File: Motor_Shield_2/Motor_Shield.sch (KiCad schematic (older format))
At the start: 49 parts, among them J1 Conn_01x08_Female, J10 Conn_01x02_Male, J11 Conn_01x02_Male, J12 Conn_01x02_Male, J13 Conn_01x02_Male, J14 Conn_01x02_Male, J15 Conn_01x02_Male, J16 Conn_01x02_Male, J17 Conn_01x02_Male, J18 Conn_01x02_Male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

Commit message: Überarbeiten das Pin Header schlecht plaziert waren
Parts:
- removed D4, D5, D6, D7: LED, Diode_SMD:D_1206_3216Metric, symbol Device:LED
- removed R22, R23, R24, R25: 2.2k, Resistor_SMD:R_1206_3216Metric_Pad1.42x1.75mm_HandSolder, symbol Device:R
- added J23: Conn_01x04_Female, Connector_PinHeader_2.54mm:PinHeader_1x04_P2.54mm_Vertical, symbol Connector:Conn_01x04_Female
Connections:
- net at J6.3 (Pin_3), U1.17 (OUT1B), U1.18 (OUT1B): now also J23.3 (Pin_3)
- net at J6.5 (Pin_5), U1.2 (OUT1A), U1.3 (OUT1A): now also J23.1 (Pin_1)
- net at J6.4 (Pin_4), U1.20 (OUT2B), U1.21 (OUT2B): now also J23.4 (Pin_4)
- net at J6.6 (Pin_6), U1.35 (OUT2A), U1.36 (OUT2A): now also J23.2 (Pin_2)
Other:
- note added: "Debug_PL Anschluss"
- note added: "J7\n\nJ12\n\nJ17\n\nJ20"
- note added: "J8\n\nJ13\n\nJ18\n\nJ21"
- note added: "J9\n\nJ14\n\nJ19\n\nJ22\n"
- note removed: "R1\n\nR4\n\nR7\n\nR10"
- note removed: "R2\n\nR5\n\nR8\n\nR11"
- note removed: "R3\n\nR6\n\nR9\n\nR12"
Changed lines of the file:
@@
 EESchema Schematic File Version 4
+LIBS:Motor_Shield-cache
 EELAYER 30 0
 EELAYER END
@@
 	6800 3850 6600 3850
 Wire Wire Line
-	6600 4050 6800 4050
-Wire Wire Line
-	6800 4050 6800 4150
-Wire Wire Line
-	6800 4150 6600 4150
-Wire Wire Line
-	6800 3000 6850 3000
-Wire Wire Line
 	8050 3000 8050 2700
 Wire Wire Line
@@
 Connection ~ 6800 3000
 Wire Wire Line
-	6800 3200 7200 3200
-Wire Wire Line
-	8150 3200 8150 2800
+	8150 3200 8150 3100
 Connection ~ 6800 3200
 Wire Wire Line
-	6800 3750 7550 3750
-Wire Wire Line
-	7900 3750 7900 2500
+	7900 3750 7900 3250
 Wire Wire Line
 	7900 2500 8150 2500
 Connection ~ 6800 3750
 Wire Wire Line
-	8000 4050 8000 2600
-Wire Wire Line
 	8000 2600 8150 2600
-Wire Wire Line
-	6800 4050 7900 4050
-Connection ~ 6800 4050
-$Comp
-L Device:LED D4
-U 1 1 5E5AB89E
-P 6850 4450
-F 0 "D4" V 6889 4333 50  0000 R CNN
-F 1 "LED" V 6798 4333 50  0000 R CNN
-F 2 "Diode_SMD:D_1206_3216Metric" H 6850 4450 50  0001 C CNN
-F 3 "~" H 6850 4450 50  0001 C CNN
-	1    6850 4450
-	0    -1   -1   0
-$EndComp
-$Comp
-L Device:R R22
-U 1 1 5E5AD872
-P 6850 4850
-F 0 "R22" V 6643 4850 50  0000 C CNN
-F 1 "2.2k" V 6734 4850 50  0000 C CNN
-F 2 "Resistor_SMD:R_1206_3216Metric_Pad1.42x1.75mm_HandSolder" V 6780 4850 50  0001 C CNN
-F 3 "~" H 6850 4850 50  0001 C CNN
-	1    6850 4850
-	-1   0    0    1
-$EndComp
-$Comp
-L power:GND #PWR019
-U 1 1 5E5AF353
-P 6850 5100
-F 0 "#PWR019" H 6850 4850 50  0001 C CNN
-F 1 "GND" H 6855 4927 50  0000 C CNN
-F 2 "" H 6850 5100 50  0001 C CNN
-F 3 "" H 6850 5100 50  0001 C CNN
-	1    6850 5100
-	1    0    0    -1
-$EndComp
-Wire Wire Line
-	6850 5100 6850 5000
-Wire Wire Line
-	6850 4700 6850 4600
-$Comp
-L Device:LED D5
-U 1 1 5E5B4D77
-P 7200 4450
-F 0 "D5" V 7239 4333 50  0000 R CNN
-F 1 "LED" V 7148 4333 50  0000 R CNN
-F 2 "Diode_SMD:D_1206_3216Metric" H 7200 4450 50  0001 C CNN
-F 3 "~" H 7200 4450 50  0001 C CNN
-	1    7200 4450
-	0    -1   -1   0
-$EndComp
-$Comp
-L Device:R R23
-U 1 1 5E5B4D7D
-P 7200 4850
-F 0 "R23" V 6993 4850 50  0000 C CNN
-F 1 "2.2k" V 7084 4850 50  0000 C CNN
-F 2 "Resistor_SMD:R_1206_3216Metric_Pad1.42x1.75mm_HandSolder" V 7130 4850 50  0001 C CNN
-F 3 "~" H 7200 4850 50  0001 C CNN
-	1    7200 4850
-	-1   0    0    1
-$EndComp
-$Comp
-L power:GND #PWR021
-U 1 1 5E5B4D83
-P 7200 5100
-F 0 "#PWR021" H 7200 4850 50  0001 C CNN
-F 1 "GND" H 7205 4927 50  0000 C CNN
-F 2 "" H 7200 5100 50  0001 C CNN
-F 3 "" H 7200 5100 50  0001 C CNN
-	1    7200 5100
-	1    0    0    -1
-$EndComp
-Wire Wire Line
-	7200 5100 7200 5000
-Wire Wire Line
-	7200 4700 7200 4600
-$Comp
-L Device:LED D6
-U 1 1 5E5B6E4B
-P 7550 4450
-F 0 "D6" V 7589 4333 50  0000 R CNN
-F 1 "LED" V 7498 4333 50  0000 R CNN
-F 2 "Diode_SMD:D_1206_3216Metric" H 7550 4450 50  0001 C CNN
-F 3 "~" H 7550 4450 50  0001 C CNN
-	1    7550 4450
-	0    -1   -1   0
-$EndComp
-$Comp
-L Device:R R24
-U 1 1 5E5B6E51
-P 7550 4850
-F 0 "R24" V 7343 4850 50  0000 C CNN
-F 1 "2.2k" V 7434 4850 50  0000 C CNN
-F 2 "Resistor_SMD:R_1206_3216Metric_Pad1.42x1.75mm_HandSolder" V 7480 4850 50  0001 C CNN
-F 3 "~" H 7550 4850 50  0001 C CNN
-	1    7550 4850
-	-1   0    0    1
-$EndComp
-$Comp
-L power:GND #PWR023
-U 1 1 5E5B6E57
-P 7550 5100
-F 0 "#PWR023" H 7550 4850 50  0001 C CNN
-F 1 "GND" H 7555 4927 50  0000 C CNN
-F 2 "" H 7550 5100 50  0001 C CNN
-F 3 "" H 7550 5100 50  0001 C CNN
-	1    7550 5100
-	1    0    0    -1
-$EndComp
-Wire Wire Line
-	7550 5100 7550 5000
-Wire Wire Line
-	7550 4700 7550 4600
-$Comp
-L Device:LED D7
-U 1 1 5E5B9165
-P 7900 4450
-F 0 "D7" V 7939 4333 50  0000 R CNN
-F 1 "LED" V 7848 4333 50  0000 R CNN
-F 2 "Diode_SMD:D_1206_3216Metric" H 7900 4450 50  0001 C CNN
-F 3 "~" H 7900 4450 50  0001 C CNN
-	1    7900 4450
-	0    -1   -1   0
-$EndComp
-$Comp
-L Device:R R25
-U 1 1 5E5B916B
-P 7900 4850
-F 0 "R25" V 7693 4850 50  0000 C CNN
-F 1 "2.2k" V 7784 4850 50  0000 C CNN
-F 2 "Resistor_SMD:R_1206_3216Metric_Pad1.42x1.75mm_HandSolder" V 7830 4850 50  0001 C CNN
-F 3 "~" H 7900 4850 50  0001 C CNN
-	1    7900 4850
-	-1   0    0    1
-$EndComp
-$Comp
-L power:GND #PWR025
-U 1 1 5E5B9171
-P 7900 5100
-F 0 "#PWR025" H 7900 4850 50  0001 C CNN
-F 1 "GND" H 7905 4927 50  0000 C CNN
-F 2 "" H 7900 5100 50  0001 C CNN
-F 3 "" H 7900 5100 50  0001 C CNN
-	1    7900 5100
-	1    0    0    -1
-$EndComp
-Wire Wire Line
-	7900 5100 7900 5000
-Wire Wire Line
-	7900 4700 7900 4600
-Wire Wire Line
-	6850 4300 6850 3000
-Connection ~ 6850 3000
-Wire Wire Line
-	6850 3000 8050 3000
-Wire Wire Line
-	7200 4300 7200 3200
-Connection ~ 7200 3200
-Wire Wire Line
-	7200 3200 8150 3200
-Wire Wire Line
-	7550 4300 7550 3750
-Connection ~ 7550 3750
-Wire Wire Line
-	7550 3750 7900 3750
-Wire Wire Line
-	7900 4300 7900 4050
-Connection ~ 7900 4050
-Wire Wire Line
-	7900 4050 8000 4050
 $Comp
 L power:GND #PWR015
@@
 Text Notes 4450 6400 0    50   ~ 0
 SPI Motor
-Text Notes 9250 5500 0    50   ~ 0
-R3\n\nR6\n\nR9\n\nR12
-Text Notes 9600 5500 0    50   ~ 0
-R2\n\nR5\n\nR8\n\nR11
-Text Notes 9950 5500 0    50   ~ 0
-R1\n\nR4\n\nR7\n\nR10
 Text Notes 9350 5800 1    50   ~ 0
 No.3
@@
 Wire Wire Line
 	1750 2150 1750 2400
+Wire Wire Line
+	6800 4150 6600 4150
+Wire Wire Line
+	6600 4050 6800 4050
+Connection ~ 6800 4050
+Wire Wire Line
+	6800 4050 6800 4150
+Wire Wire Line
+	6800 4050 8000 4050
+Wire Wire Line
+	6800 3750 7900 3750
+Wire Wire Line
+	6800 3200 8150 3200
+Wire Wire Line
+	6800 3000 8050 3000
+$Comp
+L Connector:Conn_01x04_Female J23
+U 1 1 5E62AB36
+P 8525 3100
+F 0 "J23" H 8553 3076 50  0000 L CNN
+F 1 "Conn_01x04_Female" H 8553 2985 50  0000 L CNN
+F 2 "Connector_PinHeader_2.54mm:PinHeader_1x04_P2.54mm_Vertical" H 8525 3100 50  0001 C CNN
+F 3 "~" H 8525 3100 50  0001 C CNN
+	1    8525 3100
+	1    0    0    -1
+$EndComp
+Wire Wire Line
+	8050 3000 8325 3000
+Connection ~ 8050 3000
+Wire Wire Line
+	8150 3100 8325 3100
+Connection ~ 8150 3100
+Wire Wire Line
+	8150 3100 8150 2800
+Wire Wire Line
+	8325 3300 8000 3300
+Wire Wire Line
+	8000 2600 8000 3300
+Connection ~ 8000 3300
+Wire Wire Line
+	8000 3300 8000 4050
+Wire Wire Line
+	7900 3250 8325 3250
+Wire Wire Line
+	8325 3250 8325 3200
+Connection ~ 7900 3250
+Wire Wire Line
+	7900 3250 7900 2500
+Text Notes 8650 3150 0    50   ~ 0
+Debug_PL Anschluss
+Text Notes 9950 5500 0    50   ~ 0
+J7\n\nJ12\n\nJ17\n\nJ20
+Text Notes 9600 5500 0    50   ~ 0
+J8\n\nJ13\n\nJ18\n\nJ21
+Text Notes 9275 5500 0    50   ~ 0
+J9\n\nJ14\n\nJ19\n\nJ22\n
 $EndSCHEMATC

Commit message: PCB fertig
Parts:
- removed J23: Conn_01x04_Female, Connector_PinHeader_2.54mm:PinHeader_1x04_P2.54mm_Vertical, symbol Connector:Conn_01x04_Female
- added J23: Conn_02x03_Counter_Clockwise, Connector_PinHeader_2.54mm:PinHeader_2x03_P2.54mm_Vertical, symbol Connector_Generic:Conn_02x03_Counter_Clockwise
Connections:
- net GND: now also J23.5 (Pin_5)
- net VDD: now also J23.6 (Pin_6)
- net at J6.3 (Pin_3), U1.17 (OUT1B), U1.18 (OUT1B): now also J23.4 (Pin_4)
- net at J6.5 (Pin_5), U1.2 (OUT1A), U1.3 (OUT1A): now also J23.1 (Pin_1)
- net at J6.4 (Pin_4), U1.20 (OUT2B), U1.21 (OUT2B): now also J23.3 (Pin_3)
- net at J6.6 (Pin_6), U1.35 (OUT2A), U1.36 (OUT2A): now also J23.2 (Pin_2)
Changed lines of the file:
@@
 EESchema Schematic File Version 4
-LIBS:Motor_Shield-cache
 EELAYER 30 0
 EELAYER END
@@
 	8050 2700 8150 2700
 Connection ~ 6800 3000
-Wire Wire Line
-	8150 3200 8150 3100
 Connection ~ 6800 3200
-Wire Wire Line
-	7900 3750 7900 3250
 Wire Wire Line
 	7900 2500 8150 2500
@@
 Wire Wire Line
 	6800 3000 8050 3000
-$Comp
-L Connector:Conn_01x04_Female J23
-U 1 1 5E62AB36
-P 8525 3100
-F 0 "J23" H 8553 3076 50  0000 L CNN
-F 1 "Conn_01x04_Female" H 8553 2985 50  0000 L CNN
-F 2 "Connector_PinHeader_2.54mm:PinHeader_1x04_P2.54mm_Vertical" H 8525 3100 50  0001 C CNN
-F 3 "~" H 8525 3100 50  0001 C CNN
-	1    8525 3100
-	1    0    0    -1
-$EndComp
-Wire Wire Line
-	8050 3000 8325 3000
-Connection ~ 8050 3000
-Wire Wire Line
-	8150 3100 8325 3100
-Connection ~ 8150 3100
-Wire Wire Line
-	8150 3100 8150 2800
-Wire Wire Line
-	8325 3300 8000 3300
-Wire Wire Line
-	8000 2600 8000 3300
-Connection ~ 8000 3300
-Wire Wire Line
-	8000 3300 8000 4050
-Wire Wire Line
-	7900 3250 8325 3250
-Wire Wire Line
-	8325 3250 8325 3200
-Connection ~ 7900 3250
-Wire Wire Line
-	7900 3250 7900 2500
-Text Notes 8650 3150 0    50   ~ 0
+Text Notes 9350 2700 0    50   ~ 0
 Debug_PL Anschluss
 Text Notes 9950 5500 0    50   ~ 0
@@
 Text Notes 9275 5500 0    50   ~ 0
 J9\n\nJ14\n\nJ19\n\nJ22\n
+Wire Wire Line
+	8000 2600 8000 3250
+Wire Wire Line
+	7900 2500 7900 3300
+Wire Wire Line
+	8150 2800 8150 3100
+Wire Wire Line
+	8350 3000 8050 3000
+Connection ~ 8050 3000
+Wire Wire Line
+	8350 3100 8150 3100
+Connection ~ 8150 3100
+Wire Wire Line
+	8150 3100 8150 3200
+Wire Wire Line
+	8000 3250 8350 3250
+Wire Wire Line
+	8350 3250 8350 3200
+Connection ~ 8000 3250
+Wire Wire Line
+	8000 3250 8000 4050
+Connection ~ 7900 3300
+Wire Wire Line
+	7900 3300 7900 3750
+$Comp
+L power:VDD #PWR019
+U 1 1 5E6617F8
+P 8850 2950
+F 0 "#PWR019" H 8850 2800 50  0001 C CNN
+F 1 "VDD" H 8867 3123 50  0000 C CNN
+F 2 "" H 8850 2950 50  0001 C CNN
+F 3 "" H 8850 2950 50  0001 C CNN
+	1    8850 2950
+	1    0    0    -1
+$EndComp
+$Comp
+L power:GND #PWR021
+U 1 1 5E662C51
+P 8950 3150
+F 0 "#PWR021" H 8950 2900 50  0001 C CNN
+F 1 "GND" H 8955 2977 50  0000 C CNN
+F 2 "" H 8950 3150 50  0001 C CNN
+F 3 "" H 8950 3150 50  0001 C CNN
+	1    8950 3150
+	1    0    0    -1
+$EndComp
+$Comp
+L Connector_Generic:Conn_02x03_Counter_Clockwise J23
+U 1 1 5E69254C
+P 8550 3100
+F 0 "J23" H 8600 3417 50  0000 C CNN
+F 1 "Conn_02x03_Counter_Clockwise" H 8600 3326 50  0000 C CNN
+F 2 "Connector_PinHeader_2.54mm:PinHeader_2x03_P2.54mm_Vertical" H 8550 3100 50  0001 C CNN
+F 3 "~" H 8550 3100 50  0001 C CNN
+	1    8550 3100
+	1    0    0    -1
+$EndComp
+Wire Wire Line
+	8850 3300 8850 3200
+Wire Wire Line
+	7900 3300 8850 3300
+Wire Wire Line
+	8850 2950 8850 3000
+Wire Wire Line
+	8850 3100 8950 3100
+Wire Wire Line
+	8950 3100 8950 3150
 $EndSCHEMATC

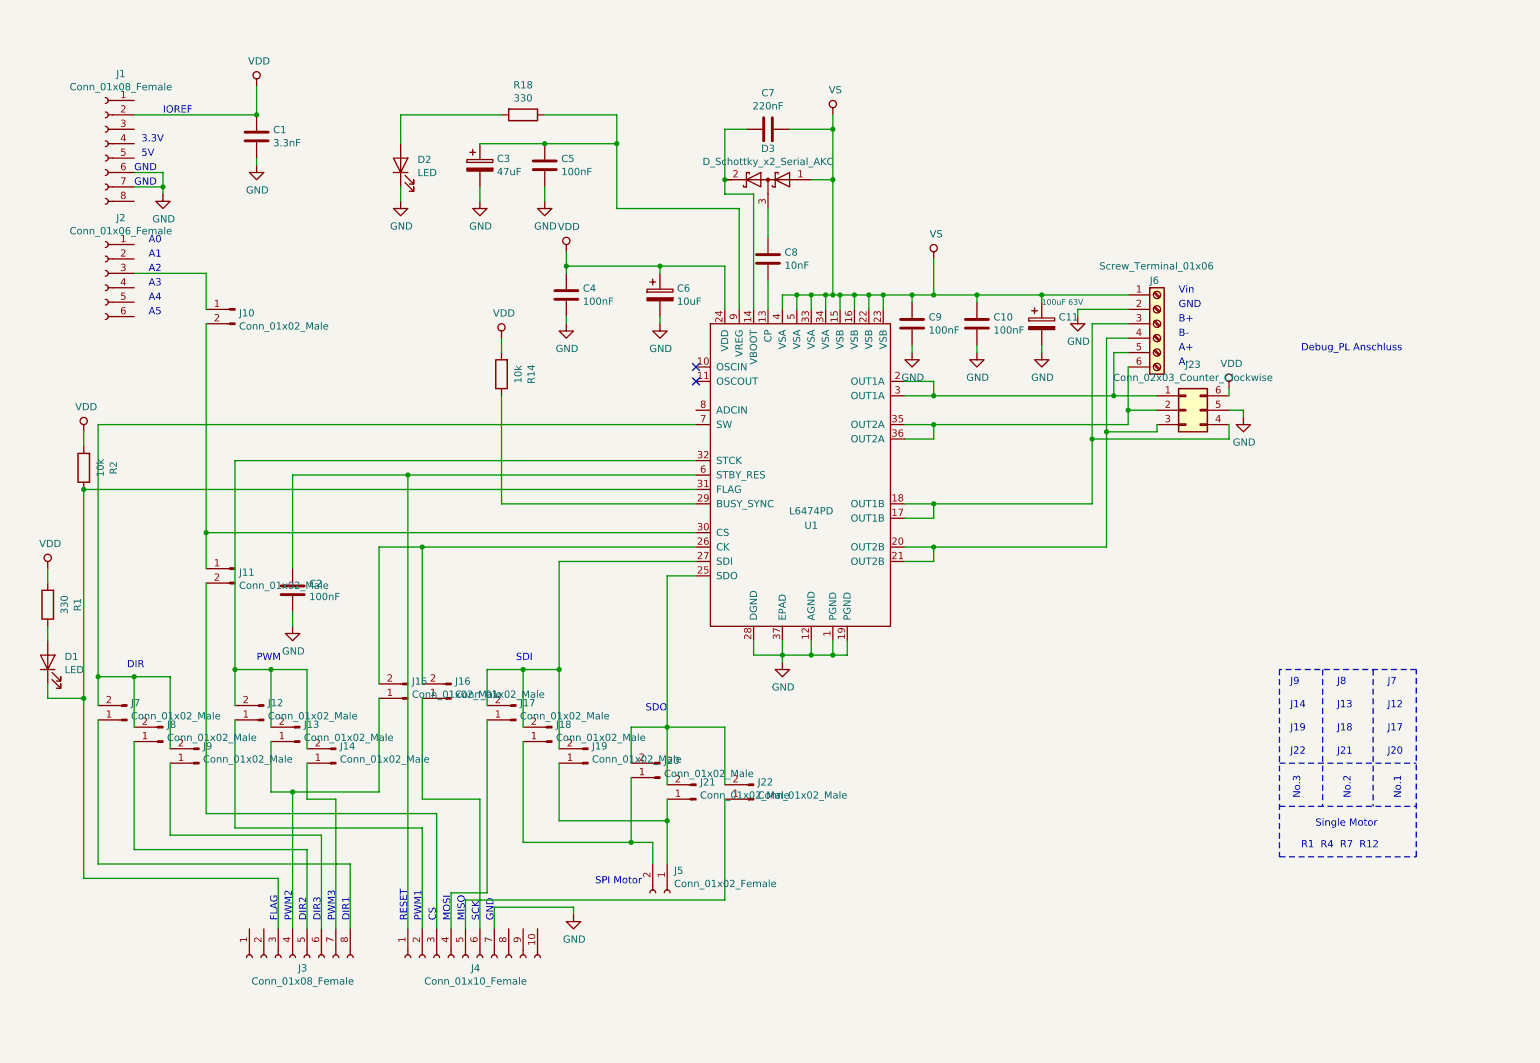
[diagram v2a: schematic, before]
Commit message: Morpho_Header hinzugefügt pcb fehlt aber noch
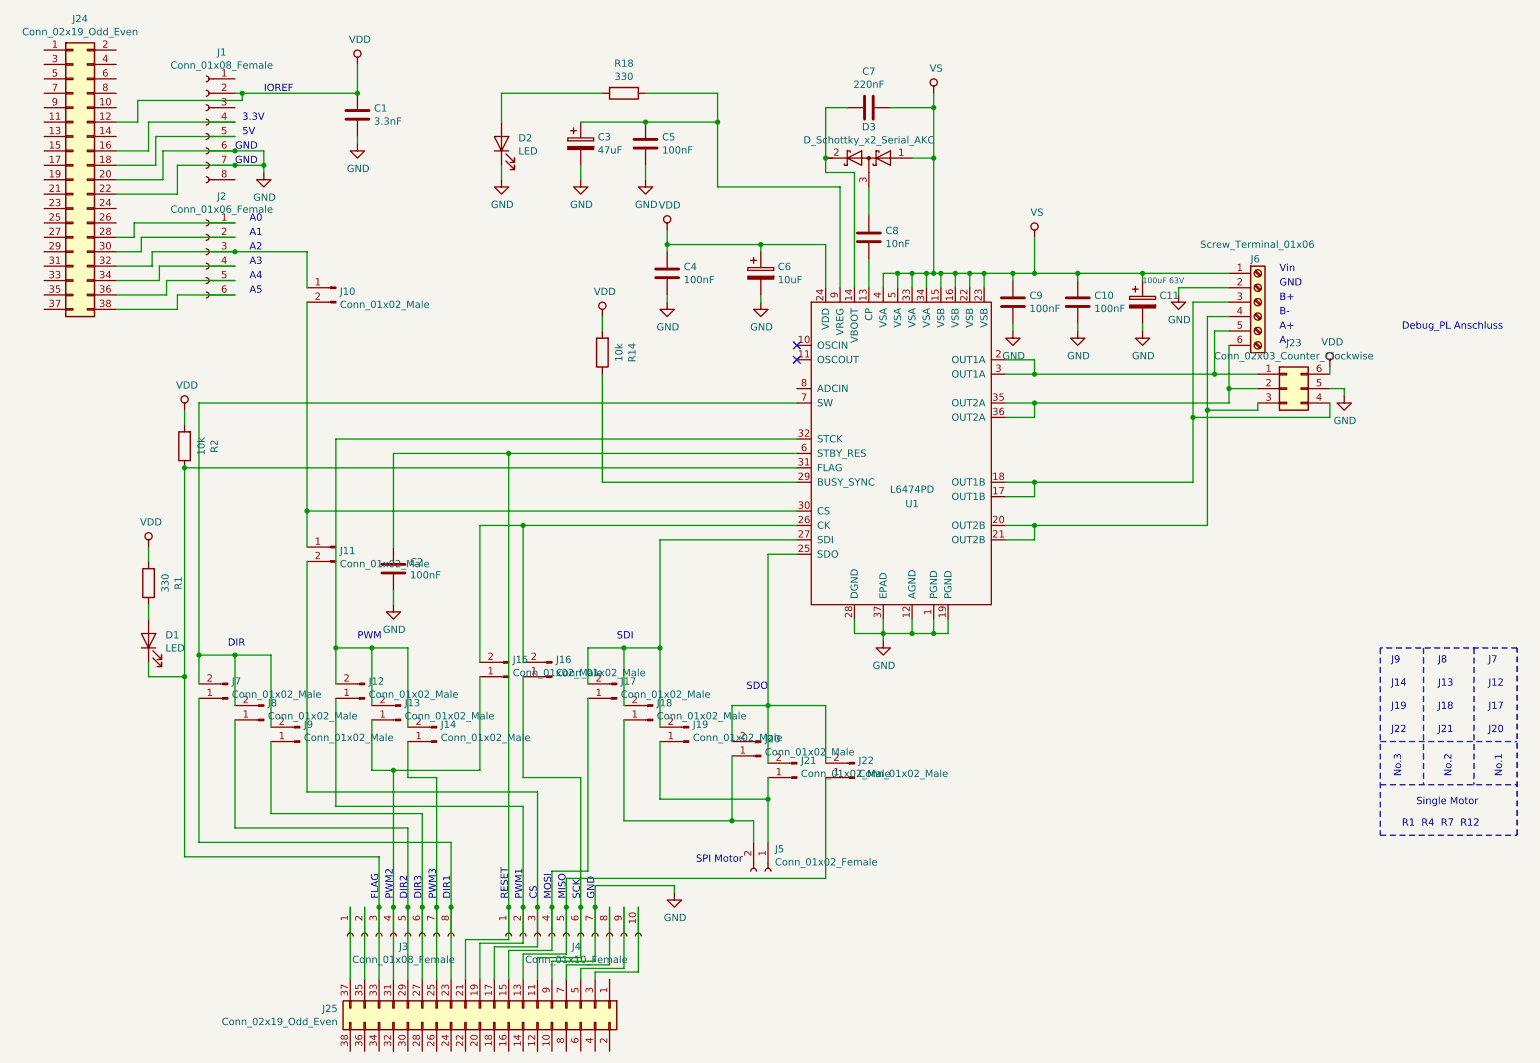
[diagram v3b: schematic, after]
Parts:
- added J24, J25: Conn_02x19_Odd_Even, Connector_PinHeader_2.54mm:PinHeader_2x19_P2.54mm_Vertical, symbol Connector_Generic:Conn_02x19_Odd_Even
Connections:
- net GND: now also J24.20 (Pin_20), J24.22 (Pin_22), J25.9 (Pin_9)
- net VDD: now also J24.12 (Pin_12)
- net at D1.1 (K), J3.3 (Pin_3), R2.1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: now also J25.33 (Pin_33)
- net at C2.1, J4.1 (Pin_1), U1.6 (STBY_RES): now also J25.21 (Pin_21)
- net at J3.8 (Pin_8), J7.1 (Pin_1): now also J25.23 (Pin_23)
- net at J3.5 (Pin_5), J8.1 (Pin_1): now also J25.29 (Pin_29)
- net at J3.6 (Pin_6), J9.1 (Pin_1): now also J25.27 (Pin_27)
- net at J1.4 (Pin_4): now also J24.16 (Pin_16)
- net at J1.5 (Pin_5): now also J24.18 (Pin_18)
- net at J2.1 (Pin_1): now also J24.28 (Pin_28)
- net at J2.2 (Pin_2): now also J24.30 (Pin_30)
- net at J10.1 (Pin_1), J2.3 (Pin_3): now also J24.32 (Pin_32)
- net at J2.4 (Pin_4): now also J24.34 (Pin_34)
- net at J2.5 (Pin_5): now also J24.36 (Pin_36)
- net at J2.6 (Pin_6): now also J24.38 (Pin_38)
- net at J12.1 (Pin_1), J4.2 (Pin_2): now also J25.19 (Pin_19)
- net at J13.1 (Pin_1), J15.1 (Pin_1), J3.4 (Pin_4): now also J25.31 (Pin_31)
- net at J14.1 (Pin_1), J3.7 (Pin_7): now also J25.25 (Pin_25)
- net at J3.1 (Pin_1): now also J25.37 (Pin_37)
- net at J3.2 (Pin_2): now also J25.35 (Pin_35)
- net at J4.10 (Pin_10): now also J25.3 (Pin_3)
- net at J11.2 (Pin_2), J4.3 (Pin_3): now also J25.17 (Pin_17)
- net at J17.1 (Pin_1), J4.4 (Pin_4): now also J25.15 (Pin_15)
- net at J22.1 (Pin_1), J4.5 (Pin_5): now also J25.13 (Pin_13)
- net at J16.1 (Pin_1), J4.6 (Pin_6): now also J25.11 (Pin_11)
- net at J4.8 (Pin_8): now also J25.7 (Pin_7)
- net at J4.9 (Pin_9): now also J25.5 (Pin_5)
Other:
- moved on the sheet: C1, C10, C11, C2, C3, C4, C5, C6, C7, C8, C9, D1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
